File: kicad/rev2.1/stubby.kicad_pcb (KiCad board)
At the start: 2 copper layers, 49.5 x 49.5 mm, 71 parts, among them IC1 ATMEGA1284-A, P1 CONN_6, P10 CONN_4, P11 CONN_6, P2 CONN_4, P3 CONN_13, P4 CONN_2, P5 CONN_1, P6 CONN_6, P7 CONN_10, P8 BATT (4.8V-6V), P9 PROG, SW1 SW_PUSH, SW2 DPDT, U1 HMC5883L, X1 CRYSTAL

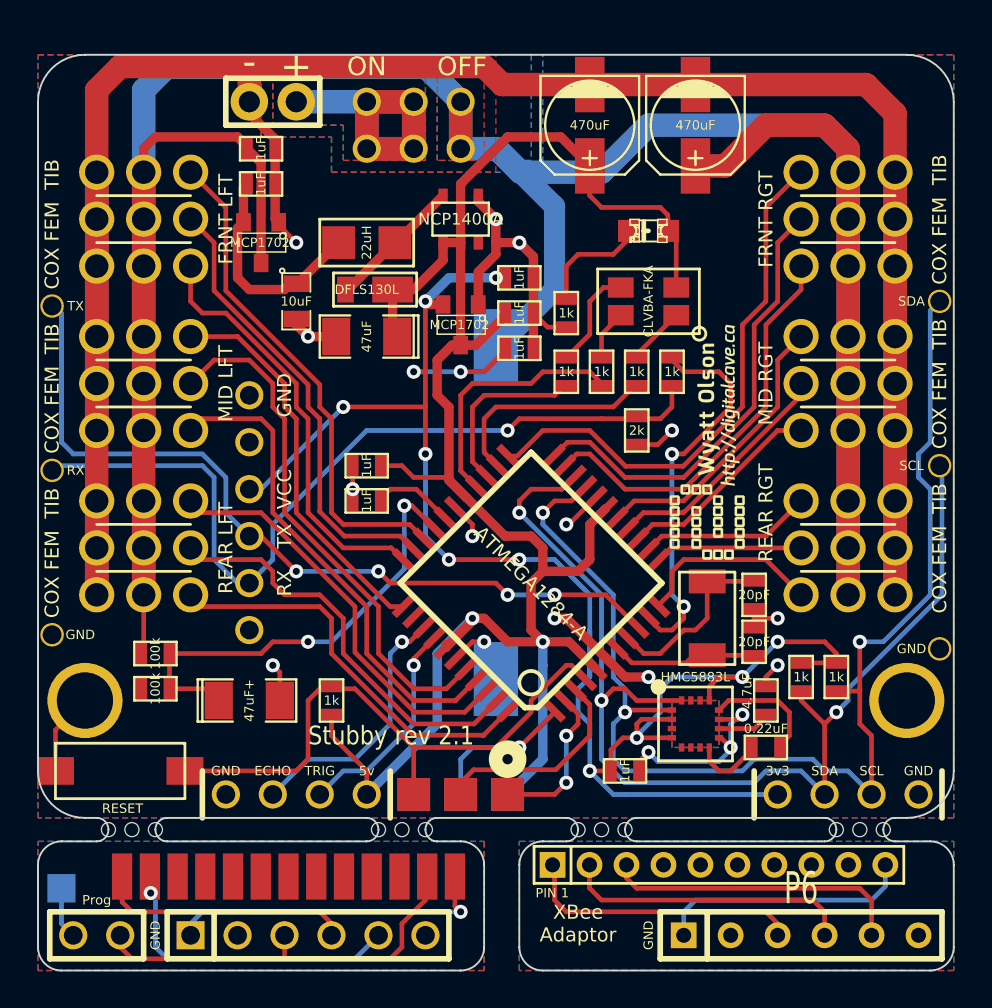
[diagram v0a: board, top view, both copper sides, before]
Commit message: Changes to schematic and routed board
Changes from Chris L's suggestions.  Includes changes to some resistor /
capacitor values, adding some more decoupling caps to AVR, adding
ferrite bead + cap to distance sensor, removed first 3.3v regulator from
power supply, etc...
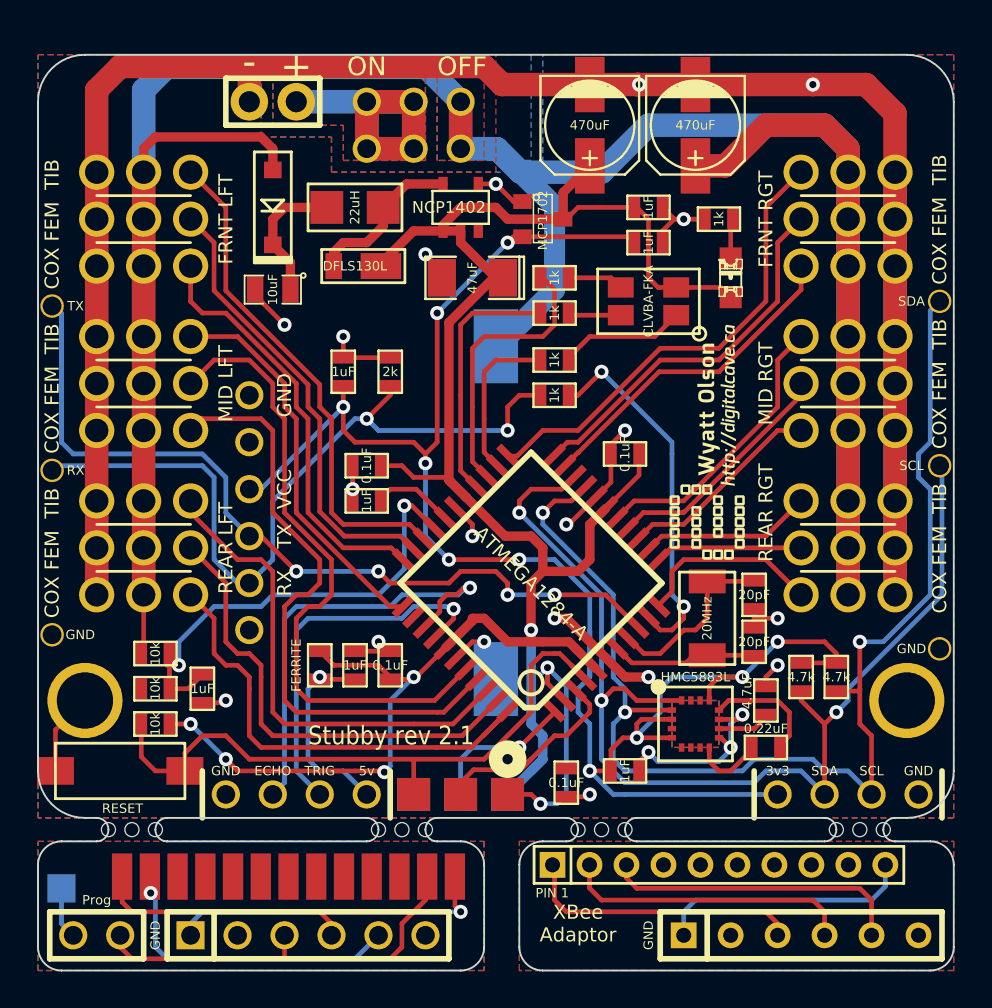
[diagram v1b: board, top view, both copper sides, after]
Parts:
- removed VR1: MCP1702, SOT23
- added C19: 0.1uF, SM0603_VALUE, F.Cu at (64.1, 54.0)
- added C20: 1uF, SM0603_VALUE, F.Cu at (52.7, 47.6)
- added D4: 1N4148W, SOD-123_DIODE, F.Cu at (48.3, 22.9)
- added L2: FERRITE, SM0603_VALUE, F.Cu at (50.8, 47.6)
- C13, C2, C4: value 1uF -> 0.1uF
- C15: value 47uF+ -> 1uF; footprint SM1206POL -> SM0603_VALUE
- R1, R2: value 1k -> 4.7k
- R3: value 1k -> 10k
- R5, R6: value 100k -> 10k
- VR3: value NCP1400A -> NCP1402
- X1: value CRYSTAL -> 20MHz
- moved C4 28.8 mm to (54.6, 47.6), turned to 90 degrees
- moved C2 16.3 mm to (53.3, 36.8), turned to 180 degrees
- moved C13 14.0 mm to (67.3, 36.2), turned to 180 degrees
- moved R8 13.7 mm to (54.6, 31.8), turned to 270 degrees
- moved R4 9.69 mm to (72.4, 23.5), turned to 0 degrees
- moved R3 9.61 mm to (41.9, 50.8), turned to 180 degrees
- moved C16 9.61 mm to (52.1, 31.8), turned to 270 degrees
- moved C5 9.03 mm to (68.6, 22.9)
- moved C3 7.24 mm to (68.6, 24.8)
- moved VR2 7.24 mm to (62.9, 23.5), turned to 270 degrees
- moved C6 6.54 mm to (59.1, 26.7)
- moved R7 6.48 mm to (63.5, 33.0), turned to 180 degrees
- moved D2 5.12 mm to (73.0, 26.7), turned to 90 degrees
- moved R10 5.12 mm to (63.5, 26.7), turned to 0 degrees
- moved R11 4.49 mm to (63.5, 31.1), turned to 0 degrees
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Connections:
- C1 pad 1: N-0000076 (its old number) -> N-0000031
- C13 pad 1: GND -> +5V
- C13 pad 2: +5V -> GND
- C15 pad 1: /ADC_BATTERY_METER -> GND
- C15 pad 2: GND -> /ADC_BATTERY_METER
- C2 pad 1: N-0000076 (its old number) -> +5V
- C4 pad 1: +BATT -> +5V
- L1 pad 1: N-0000076 (its old number) -> N-0000031
- P10 pad 1: +5V -> N-0000032
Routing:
- net +5V: track 109.0 -> 122.4 mm, vias 2 -> 5
- net N-0000076 (its old number): track 12.1 -> 0.00 mm
- net N-0000032: track 0.00 -> 10.7 mm, vias 0 -> 1
- net /DIST_ECHO: track 14.2 -> 24.1 mm
- net /DIST_TRIG: track 11.9 -> 20.4 mm
- net N-0000031: track 0.00 -> 7.39 mm
- net GND: track 209.2 -> 202.5 mm, vias 17 -> 22
- net /PWM06: track 26.7 -> 33.2 mm
- net /PWM07: track 28.5 -> 34.7 mm
- net /LED_BL: track 9.68 -> 15.2 mm
- net /MISO: track 8.51 -> 13.7 mm
- net /PWM12: track 23.3 -> 28.2 mm
- net /PWM03: track 29.4 -> 25.2 mm
- net /PWM04: track 24.7 -> 20.6 mm
- net /PWM05: track 22.2 -> 18.1 mm
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
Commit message: re-annotated schematic
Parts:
- renumbered C12 to C10, C13 to C11, C2 to C12, C4 to C13, C19 to C14, C14 to C15, C15 to C16, C20 to C17, C16 to C18, C17 to C19, C3 to C2, C18 to C20, C5 to C3, C6 to C4, C7 to C5, C8 to C6, C9 to C7, C10 to C8, C11 to C9, D4 to D1, D1 to D2, D2 to D3, D3 to D4, VR2 to VR1, VR3 to VR2
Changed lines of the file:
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@@
     (links 186)
     (no_connects 0)
-    (area 35.509999 14.554999 85.140001 64.185001)
+    (area 23.115001 13.74 86.865177 70.645)
     (thickness 1.6)
     (drawings 79)
@@
   (title_block
     (title "Stubby Controller")
-    (rev 2.0)
+    (rev 2.1)
     (company DigitalCave)
   )
@@
     (at 62.865 23.495 270)
     (tags SOT23)
-    (fp_text reference VR2 (at 1.99898 -0.09906 360) (layer F.SilkS) hide
+    (fp_text reference VR1 (at 1.99898 -0.09906 360) (layer F.SilkS) hide
       (effects (font (size 0.762 0.762) (thickness 0.11938)))
     )
@@
     (at 74.295 46.355 270)
     (attr smd)
-    (fp_text reference C10 (at 0 0 270) (layer F.SilkS) hide
+    (fp_text reference C8 (at 0 0 270) (layer F.SilkS) hide
       (effects (font (size 0.508 0.508) (thickness 0.1143)))
     )
@@
     (at 74.295 43.815 90)
     (attr smd)
-    (fp_text reference C11 (at 0 0 90) (layer F.SilkS) hide
+    (fp_text reference C9 (at 0 0 90) (layer F.SilkS) hide
       (effects (font (size 0.508 0.508) (thickness 0.1143)))
     )
@@
     (at 53.34 38.735)
     (attr smd)
-    (fp_text reference C8 (at 0 0) (layer F.SilkS) hide
+    (fp_text reference C6 (at 0 0) (layer F.SilkS) hide
       (effects (font (size 0.508 0.508) (thickness 0.1143)))
     )
@@
     (at 54.61 47.625 90)
     (attr smd)
-    (fp_text reference C4 (at 0 0 90) (layer F.SilkS) hide
+    (fp_text reference C13 (at 0 0 90) (layer F.SilkS) hide
       (effects (font (size 0.508 0.508) (thickness 0.1143)))
     )
@@
     (at 53.34 36.83 180)
     (attr smd)
-    (fp_text reference C2 (at 0 0 180) (layer F.SilkS) hide
+    (fp_text reference C12 (at 0 0 180) (layer F.SilkS) hide
       (effects (font (size 0.508 0.508) (thickness 0.1143)))
     )
@@
     (tags "LED 0805 SMD")
     (attr smd)
-    (fp_text reference D2 (at 0 -1.27 90) (layer F.SilkS) hide
+    (fp_text reference D3 (at 0 -1.27 90) (layer F.SilkS) hide
       (effects (font (size 0.762 0.762) (thickness 0.127)))
     )
@@
     (at 58.42 22.86)
     (attr smd)
-    (fp_text reference VR3 (at 2.19964 -0.29972 270) (layer F.SilkS) hide
+    (fp_text reference VR2 (at 2.19964 -0.29972 270) (layer F.SilkS) hide
       (effects (font (size 0.635 0.635) (thickness 0.127)))
     )
@@
     (at 59.055 26.67 180)
     (attr smd)
-    (fp_text reference C6 (at 0 0 180) (layer F.SilkS) hide
+    (fp_text reference C4 (at 0 0 180) (layer F.SilkS) hide
       (effects (font (size 0.762 0.762) (thickness 0.127)))
     )
@@
     (at 52.705 26.035)
     (attr smd)
-    (fp_text reference D1 (at 0 0) (layer F.SilkS) hide
+    (fp_text reference D2 (at 0 0) (layer F.SilkS) hide
       (effects (font (size 0.508 0.4572) (thickness 0.1143)))
     )
@@
   (module 4-PLCC (layer F.Cu)
     (at 68.58 27.94 180)
-    (fp_text reference D3 (at 0 -2.5 180) (layer F.SilkS) hide
+    (fp_text reference D4 (at 0 -2.5 180) (layer F.SilkS) hide
       (effects (font (size 1 1) (thickness 0.15)))
     )
@@
     (at 67.31 36.195 180)
     (attr smd)
-    (fp_text reference C13 (at 0 0 180) (layer F.SilkS) hide
+    (fp_text reference C11 (at 0 0 180) (layer F.SilkS) hide
       (effects (font (size 0.508 0.508) (thickness 0.1143)))
     )
@@
     (at 52.07 31.75 270)
     (attr smd)
-    (fp_text reference C16 (at 0 0 270) (layer F.SilkS) hide
+    (fp_text reference C18 (at 0 0 270) (layer F.SilkS) hide
       (effects (font (size 0.508 0.508) (thickness 0.1143)))
     )
@@
     (at 74.93 49.53 90)
     (attr smd)
-    (fp_text reference C9 (at 0 0 90) (layer F.SilkS) hide
+    (fp_text reference C7 (at 0 0 90) (layer F.SilkS) hide
       (effects (font (size 0.508 0.508) (thickness 0.1143)))
     )
@@
     (at 74.93 52.07)
     (attr smd)
-    (fp_text reference C12 (at 0 0) (layer F.SilkS) hide
+    (fp_text reference C10 (at 0 0) (layer F.SilkS) hide
       (effects (font (size 0.508 0.508) (thickness 0.1143)))
     )
@@
     (at 68.58 24.765)
     (attr smd)
-    (fp_text reference C3 (at 0 0) (layer F.SilkS) hide
+    (fp_text reference C2 (at 0 0) (layer F.SilkS) hide
       (effects (font (size 0.508 0.508) (thickness 0.1143)))
     )
@@
     (at 68.58 22.86)
     (attr smd)
-    (fp_text reference C5 (at 0 0) (layer F.SilkS) hide
+    (fp_text reference C3 (at 0 0) (layer F.SilkS) hide
       (effects (font (size 0.508 0.508) (thickness 0.1143)))
     )
@@
     (at 67.31 53.34)
     (attr smd)
-    (fp_text reference C14 (at 0 0) (layer F.SilkS) hide
+    (fp_text reference C15 (at 0 0) (layer F.SilkS) hide
       (effects (font (size 0.508 0.508) (thickness 0.1143)))
     )
@@
     (at 65.405 18.415 270)
     (descr "SMT capacitor, aluminium electrolytic, 5x5.3")
-    (fp_text reference C7 (at 0 -3.175 270) (layer F.SilkS) hide
+    (fp_text reference C5 (at 0 -3.175 270) (layer F.SilkS) hide
       (effects (font (size 0.50038 0.50038) (thickness 0.11938)))
     )
@@
     (at 60.325 39.37 90)
     (descr "SMT capacitor, aluminium electrolytic, 10x10")
-    (fp_text reference C17 (at 0 5.842 90) (layer B.SilkS)
+    (fp_text reference C19 (at 0 5.842 90) (layer B.SilkS)
       (effects (font (size 0.50038 0.50038) (thickness 0.11938)) (justify mirror))
     )
@@
     (at 71.12 18.415 270)
     (descr "SMT capacitor, aluminium electrolytic, 5x5.3")
-    (fp_text reference C18 (at 0 -3.175 270) (layer F.SilkS) hide
+    (fp_text reference C20 (at 0 -3.175 270) (layer F.SilkS) hide
       (effects (font (size 0.50038 0.50038) (thickness 0.11938)))
     )
@@
   (module SOD-123_DIODE (layer F.Cu)
     (at 48.26 22.86 270)
-    (fp_text reference D4 (at 0 -4 270) (layer F.SilkS) hide
+    (fp_text reference D1 (at 0 -4 270) (layer F.SilkS) hide
       (effects (font (size 1 1) (thickness 0.15)))
     )
@@
     (at 64.135 53.975 270)
     (attr smd)
-    (fp_text reference C19 (at 0 0 270) (layer F.SilkS) hide
+    (fp_text reference C14 (at 0 0 270) (layer F.SilkS) hide
       (effects (font (size 0.508 0.508) (thickness 0.1143)))
     )
@@
     (at 44.45 48.895 90)
     (attr smd)
-    (fp_text reference C15 (at 0 0 90) (layer F.SilkS) hide
+    (fp_text reference C16 (at 0 0 90) (layer F.SilkS) hide
       (effects (font (size 0.508 0.508) (thickness 0.1143)))
     )
@@
     (at 52.705 47.625 90)
     (attr smd)
-    (fp_text reference C20 (at 0 0 90) (layer F.SilkS) hide
+    (fp_text reference C17 (at 0 0 90) (layer F.SilkS) hide
       (effects (font (size 0.508 0.508) (thickness 0.1143)))
     )

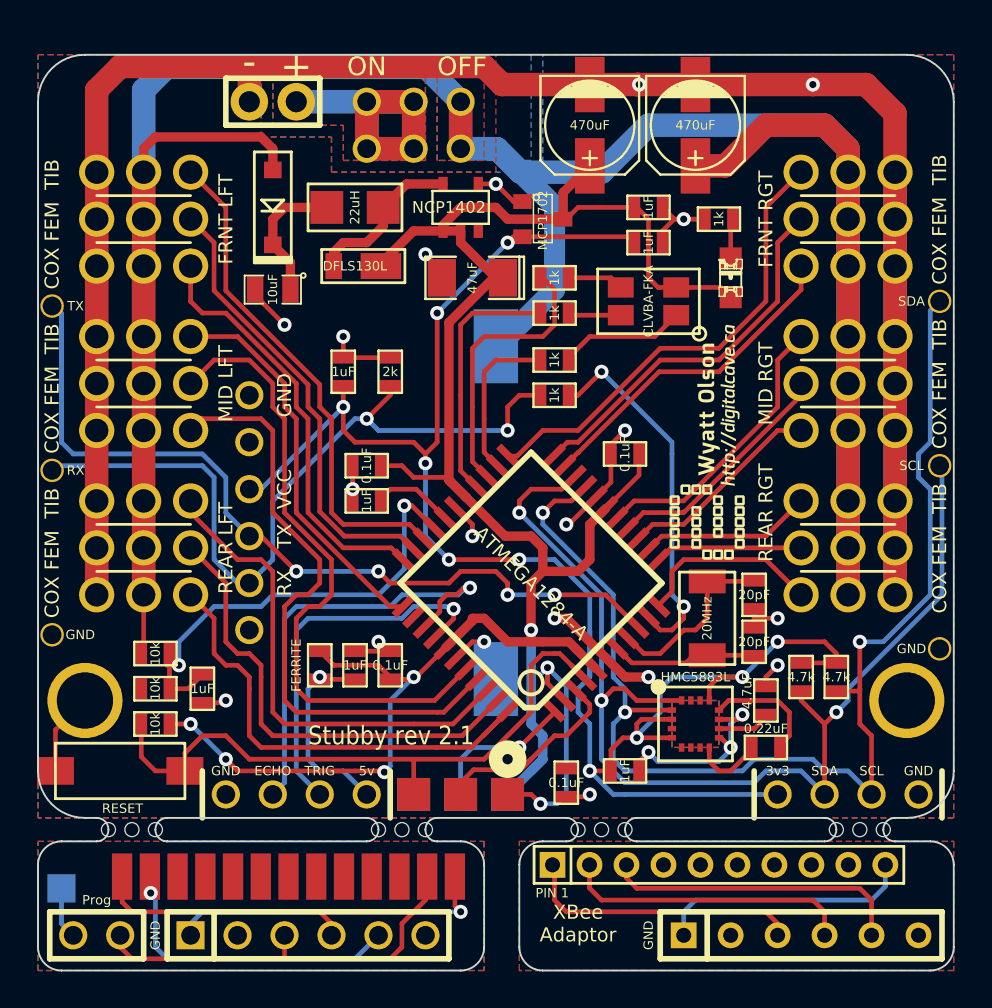
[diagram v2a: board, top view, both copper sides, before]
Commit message: Reworking boost regulator routing
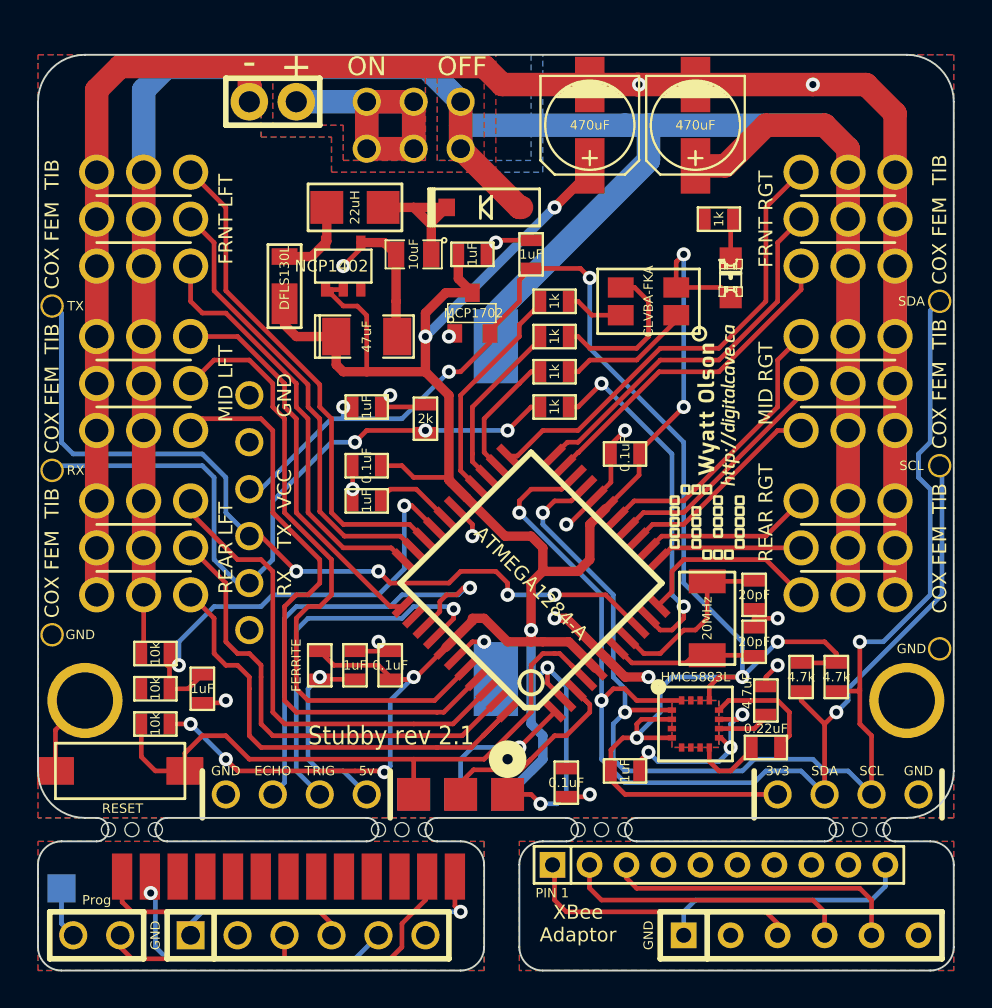
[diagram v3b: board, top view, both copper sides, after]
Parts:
- moved D1 11.4 mm to (59.7, 22.9), turned to 180 degrees
- moved C3 9.86 mm to (59.1, 25.4)
- moved C1 7.85 mm to (55.9, 25.4)
- moved VR2 7.10 mm to (52.1, 26.0)
- moved C4 6.54 mm to (53.3, 29.8), turned to 0 degrees
- moved C2 6.38 mm to (62.2, 25.4), turned to 90 degrees
- moved VR1 6.35 mm to (59.1, 28.6), turned to 0 degrees
- moved D2 3.86 mm to (48.9, 26.7), turned to 270 degrees
- moved R8 3.18 mm to (56.5, 34.3)
- moved R10 3.17 mm to (63.5, 29.8)
- moved C18 2.29 mm to (53.3, 33.7), turned to 180 degrees
- moved R11 0.64 mm to (63.5, 31.8)
- moved R7 0.63 mm to (63.5, 33.7)
- moved R9 0.63 mm to (63.5, 27.9)
- turned L1 to 180 degrees
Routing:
- net +5V: track 122.4 -> 139.0 mm, vias 5 -> 9
- net +3.3V: track 100.4 -> 87.3 mm, vias 10 -> 6
- net /LED_BL: track 15.2 -> 9.47 mm
- net /LED_BL_R: track 3.03 -> 8.56 mm
- net N-0000019: track 8.79 -> 4.47 mm
- net /MODULE_RX: track 41.4 -> 37.6 mm, vias 2 -> 3
- net +BATT: track 175.7 -> 172.6 mm
- net /LED_RD: track 8.75 -> 7.00 mm
- net /LED_GR: track 13.8 -> 12.2 mm
- net /AVR_TX: track 20.1 -> 19.4 mm
- net GND: track 202.5 -> 202.6 mm, vias 22 -> 21
